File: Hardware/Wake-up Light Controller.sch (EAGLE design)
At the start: 47 parts, among them IC1 ST1S10, IC2 HT7333, IC3 DS3231/SO, IC4 ATMEGA328P_TQFP, J1 AVR-ISP, J2 Debug, J3 CR1632_3V, Q1 BSS138, Q2 BSS138, Q3 FDN306P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

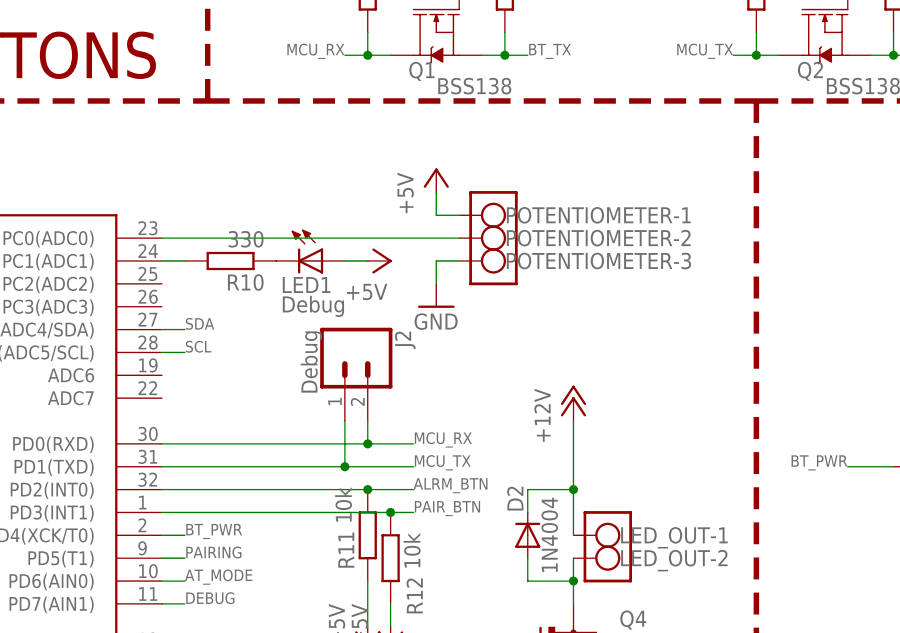
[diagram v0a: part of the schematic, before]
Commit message: Isolate ADC trace from switching PSU
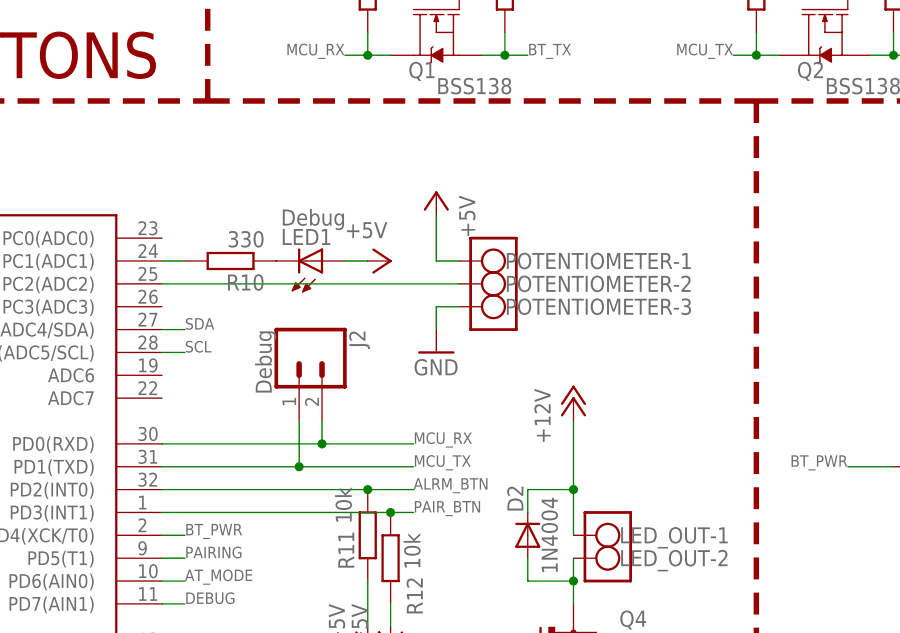
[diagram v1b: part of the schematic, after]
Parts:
- LOGO1: value OSHW-LOGOL-COPPER -> OSHW-LOGOM-COPPER; device SparkFun-Aesthetics:OSHW-LOGOL-COPPER -> SparkFun-Aesthetics:OSHW-LOGOM-COPPER
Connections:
- net N$11: now also IC4.PC2(ADC2); no longer IC4.PC0(ADC0)
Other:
- moved on the sheet: J2, LED1, POTENTIOMETER-1, POTENTIOMETER-2, POTENTIOMETER-3
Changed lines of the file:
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@@
 <part name="P+7" library="supply1" library_urn="urn:adsk.eagle:library:371" deviceset="+5V" device=""/>
 <part name="FRAME1" library="frames" library_urn="urn:adsk.eagle:library:229" deviceset="A4L-LOC" device=""/>
-<part name="LOGO1" library="SparkFun-Aesthetics" library_urn="urn:adsk.eagle:library:507" deviceset="OSHW-LOGO" device="L-COPPER" package3d_urn="urn:adsk.eagle:package:37117/1" value="OSHW-LOGOL-COPPER"/>
+<part name="LOGO1" library="SparkFun-Aesthetics" library_urn="urn:adsk.eagle:library:507" deviceset="OSHW-LOGO" device="M-COPPER" package3d_urn="urn:adsk.eagle:package:37119/1" value="OSHW-LOGOM-COPPER"/>
 <part name="GND7" library="supply1" deviceset="GND" device=""/>
 <part name="+3V35" library="supply1" library_urn="urn:adsk.eagle:library:371" deviceset="+3V3" device=""/>
@@
 <wire x1="-14.224" y1="160.02" x2="-14.224" y2="167.64" width="0.3048" layer="94"/>
 <wire x1="-14.224" y1="167.64" x2="-8.89" y2="167.64" width="0.3048" layer="94"/>
-<wire x1="92.71" y1="96.52" x2="92.71" y2="86.36" width="0.3048" layer="94"/>
-<wire x1="92.71" y1="86.36" x2="97.79" y2="86.36" width="0.3048" layer="94"/>
-<wire x1="97.79" y1="86.36" x2="97.79" y2="96.52" width="0.3048" layer="94"/>
-<wire x1="97.79" y1="96.52" x2="92.71" y2="96.52" width="0.3048" layer="94"/>
+<wire x1="92.71" y1="91.44" x2="92.71" y2="81.28" width="0.3048" layer="94"/>
+<wire x1="92.71" y1="81.28" x2="97.79" y2="81.28" width="0.3048" layer="94"/>
+<wire x1="97.79" y1="81.28" x2="97.79" y2="91.44" width="0.3048" layer="94"/>
+<wire x1="97.79" y1="91.44" x2="92.71" y2="91.44" width="0.3048" layer="94"/>
 <wire x1="105.41" y1="60.96" x2="110.49" y2="60.96" width="0.3048" layer="94"/>
 <wire x1="110.49" y1="60.96" x2="110.49" y2="53.34" width="0.3048" layer="94"/>
@@
 <instance part="C10" gate="G$1" x="-2.54" y="45.72"/>
 <instance part="P+9" gate="1" x="-2.54" y="50.8"/>
-<instance part="GND4" gate="1" x="88.9" y="83.82"/>
-<instance part="P+7" gate="1" x="88.9" y="99.06"/>
+<instance part="GND4" gate="1" x="88.9" y="78.74"/>
+<instance part="P+7" gate="1" x="88.9" y="96.52" rot="MR0"/>
 <instance part="FRAME1" gate="G$1" x="-27.94" y="7.62"/>
 <instance part="LOGO1" gate="G$1" x="146.304" y="24.638"/>
@@
 <instance part="PWR_IN" gate="-1" x="-12.7" y="162.56"/>
 <instance part="PWR_IN" gate="-2" x="-12.7" y="165.1"/>
-<instance part="POTENTIOMETER" gate="-1" x="96.52" y="93.98" rot="MR0"/>
-<instance part="POTENTIOMETER" gate="-2" x="96.52" y="91.44" rot="MR0"/>
-<instance part="POTENTIOMETER" gate="-3" x="96.52" y="88.9" rot="MR0"/>
+<instance part="POTENTIOMETER" gate="-1" x="96.52" y="88.9" rot="MR0"/>
+<instance part="POTENTIOMETER" gate="-2" x="96.52" y="86.36" rot="MR0"/>
+<instance part="POTENTIOMETER" gate="-3" x="96.52" y="83.82" rot="MR0"/>
 <instance part="LED_OUT" gate="-1" x="109.22" y="58.42" rot="MR0"/>
 <instance part="LED_OUT" gate="-2" x="109.22" y="55.88" rot="MR0"/>
@@
 <instance part="P+11" gate="1" x="144.78" y="177.8"/>
 <instance part="R10" gate="G$1" x="66.04" y="88.9" rot="R180"/>
-<instance part="LED1" gate="G$1" x="76.2" y="88.9" rot="R270"/>
-<instance part="P+12" gate="1" x="83.82" y="88.9" rot="MR90"/>
-<instance part="J2" gate="G$1" x="78.74" y="78.74" rot="R270"/>
+<instance part="LED1" gate="G$1" x="76.2" y="88.9" rot="MR90"/>
+<instance part="P+12" gate="1" x="83.82" y="88.9" rot="R270"/>
+<instance part="J2" gate="G$1" x="73.66" y="78.74" rot="R270"/>
 <instance part="R11" gate="G$1" x="81.28" y="58.42" smashed="yes" rot="R90">
 <attribute name="NAME" x="79.7814" y="54.61" size="1.778" layer="95" rot="R90"/>
@@
 <segment>
 <pinref part="GND4" gate="1" pin="GND"/>
-<wire x1="91.44" y1="88.9" x2="88.9" y2="88.9" width="0.1524" layer="91"/>
-<wire x1="88.9" y1="88.9" x2="88.9" y2="86.36" width="0.1524" layer="91"/>
+<wire x1="91.44" y1="83.82" x2="88.9" y2="83.82" width="0.1524" layer="91"/>
+<wire x1="88.9" y1="83.82" x2="88.9" y2="81.28" width="0.1524" layer="91"/>
 <pinref part="POTENTIOMETER" gate="-3" pin="KL"/>
 </segment>
@@
 <segment>
 <pinref part="IC4" gate="U$1" pin="PD1(TXD)"/>
-<wire x1="58.42" y1="66.04" x2="78.74" y2="66.04" width="0.1524" layer="91"/>
+<wire x1="58.42" y1="66.04" x2="73.66" y2="66.04" width="0.1524" layer="91"/>
 <label x="86.36" y="66.04" size="1.27" layer="95"/>
-<wire x1="78.74" y1="66.04" x2="86.36" y2="66.04" width="0.1524" layer="91"/>
-<wire x1="78.74" y1="71.12" x2="78.74" y2="66.04" width="0.1524" layer="91"/>
-<junction x="78.74" y="66.04"/>
+<wire x1="73.66" y1="66.04" x2="86.36" y2="66.04" width="0.1524" layer="91"/>
+<wire x1="73.66" y1="71.12" x2="73.66" y2="66.04" width="0.1524" layer="91"/>
+<junction x="73.66" y="66.04"/>
 <pinref part="J2" gate="G$1" pin="1"/>
 </segment>
@@
 <segment>
 <pinref part="P+7" gate="1" pin="+5V"/>
-<wire x1="91.44" y1="93.98" x2="88.9" y2="93.98" width="0.1524" layer="91"/>
-<wire x1="88.9" y1="93.98" x2="88.9" y2="96.52" width="0.1524" layer="91"/>
+<wire x1="91.44" y1="88.9" x2="88.9" y2="88.9" width="0.1524" layer="91"/>
+<wire x1="88.9" y1="88.9" x2="88.9" y2="93.98" width="0.1524" layer="91"/>
 <pinref part="POTENTIOMETER" gate="-1" pin="KL"/>
 </segment>
@@
 </segment>
 </net>
-<net name="N$11" class="0">
-<segment>
-<pinref part="IC4" gate="U$1" pin="PC0(ADC0)"/>
-<wire x1="58.42" y1="91.44" x2="91.44" y2="91.44" width="0.1524" layer="91"/>
-<pinref part="POTENTIOMETER" gate="-2" pin="KL"/>
-</segment>
-</net>
 <net name="AT_MODE" class="0">
 <segment>
@@
 <segment>
 <pinref part="IC4" gate="U$1" pin="PD0(RXD)"/>
-<wire x1="58.42" y1="68.58" x2="81.28" y2="68.58" width="0.1524" layer="91"/>
+<wire x1="58.42" y1="68.58" x2="76.2" y2="68.58" width="0.1524" layer="91"/>
 <label x="86.36" y="68.58" size="1.27" layer="95"/>
-<wire x1="81.28" y1="68.58" x2="86.36" y2="68.58" width="0.1524" layer="91"/>
-<junction x="81.28" y="68.58"/>
+<wire x1="76.2" y1="68.58" x2="86.36" y2="68.58" width="0.1524" layer="91"/>
+<junction x="76.2" y="68.58"/>
 <pinref part="J2" gate="G$1" pin="2"/>
-<wire x1="81.28" y1="68.58" x2="81.28" y2="71.12" width="0.1524" layer="91"/>
+<wire x1="76.2" y1="68.58" x2="76.2" y2="71.12" width="0.1524" layer="91"/>
 </segment>
 <segment>
@@
 </segment>
 </net>
+<net name="N$11" class="0">
+<segment>
+<pinref part="IC4" gate="U$1" pin="PC2(ADC2)"/>
+<pinref part="POTENTIOMETER" gate="-2" pin="KL"/>
+<wire x1="58.42" y1="86.36" x2="91.44" y2="86.36" width="0.1524" layer="91"/>
+</segment>
+</net>
